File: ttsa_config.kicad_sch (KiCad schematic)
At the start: 11 parts, among them J7 Conn_01x02, SW3 B3U-1000P, SW3 SW_DIP_x09

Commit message: Friendlier sort of scan drive bits, and more doc
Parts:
- R21: now not fitted
- R21: now fitted
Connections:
- net SCS.DRV_{0}: now also R21.1, R21.2; no longer R21.1, R21.2
- net SCS.DRV_{1}: now also R21.1, R21.2; no longer R21.1, R21.2
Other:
- note added: "debounced, 'cause I'm a nice guy"
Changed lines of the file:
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@@
     (effects (font (size 0.8 0.8) (thickness 0.16) bold) (justify left bottom))
+  )
+  (text "debounced, 'cause\nI'm a nice guy" (at 250.19 77.47 90)
+    (effects (font (size 0.8 0.8)) (justify left bottom))
   )
   (text "Latch slow clock\ndivider.  When this is \npulsed, the value present\non in* pins is used to\nconfigure the slow clock\ndivider--neat."
@@
     (effects (font (size 2 2)) (justify left bottom))
   )
-  (label "SCS.setdiv" (at 231.14 76.2 90)
-    (effects (font (size 1.27 1.27)) (justify left bottom))
-  )
-  (label "SCS.DRV_{1}" (at 203.2 76.2 90) (fields_autoplaced)
+  (label "SCS.setdiv" (at 231.14 76.2 90) (fields_autoplaced)
+    (effects (font (size 1.27 1.27)) (justify left bottom))
+  )
+  (label "SCS.DRV_{1}" (at 200.66 76.2 90) (fields_autoplaced)
     (effects (font (size 1.27 1.27)) (justify left bottom))
   )
@@
     (effects (font (size 1.27 1.27)) (justify left bottom))
   )
-  (label "SCS.slowclk" (at 215.9 76.2 90)
+  (label "SCS.slowclk" (at 215.9 76.2 90) (fields_autoplaced)
     (effects (font (size 1.27 1.27)) (justify left bottom))
   )
@@
     (effects (font (size 1.27 1.27)) (justify left bottom))
   )
-  (label "SCS.DRV_{0}" (at 200.66 76.2 90) (fields_autoplaced)
+  (label "SCS.DRV_{0}" (at 203.2 76.2 90) (fields_autoplaced)
     (effects (font (size 1.27 1.27)) (justify left bottom))
   )
@@
   )
   (symbol (lib_id "Device:R_Small") (at 195.58 88.9 180) (unit 1)
-    (in_bom yes) (on_board yes) (dnp no) (fields_autoplaced)
+    (in_bom yes) (on_board yes) (dnp yes) (fields_autoplaced)
     (property "Reference" "R21" (at 194.0814 87.6879 0)
       (effects (font (size 1.27 1.27)) (justify left))
@@
   )
   (symbol (lib_id "Device:R_Small") (at 208.28 88.9 180) (unit 1)
-    (in_bom yes) (on_board yes) (dnp yes) (fields_autoplaced)
+    (in_bom yes) (on_board yes) (dnp no) (fields_autoplaced)
     (property "Reference" "R21" (at 209.7786 87.6879 0)
       (effects (font (size 1.27 1.27)) (justify right))
@@
   )
   (symbol (lib_id "Device:R_Small") (at 195.58 81.28 180) (unit 1)
-    (in_bom yes) (on_board yes) (dnp yes) (fields_autoplaced)
+    (in_bom yes) (on_board yes) (dnp no) (fields_autoplaced)
     (property "Reference" "R21" (at 194.0814 80.0679 0)
       (effects (font (size 1.27 1.27)) (justify left))
@@
   )
   (symbol (lib_id "Device:R_Small") (at 208.28 81.28 180) (unit 1)
-    (in_bom yes) (on_board yes) (dnp no) (fields_autoplaced)
+    (in_bom yes) (on_board yes) (dnp yes) (fields_autoplaced)
     (property "Reference" "R21" (at 209.7786 80.0679 0)
       (effects (font (size 1.27 1.27)) (justify right))

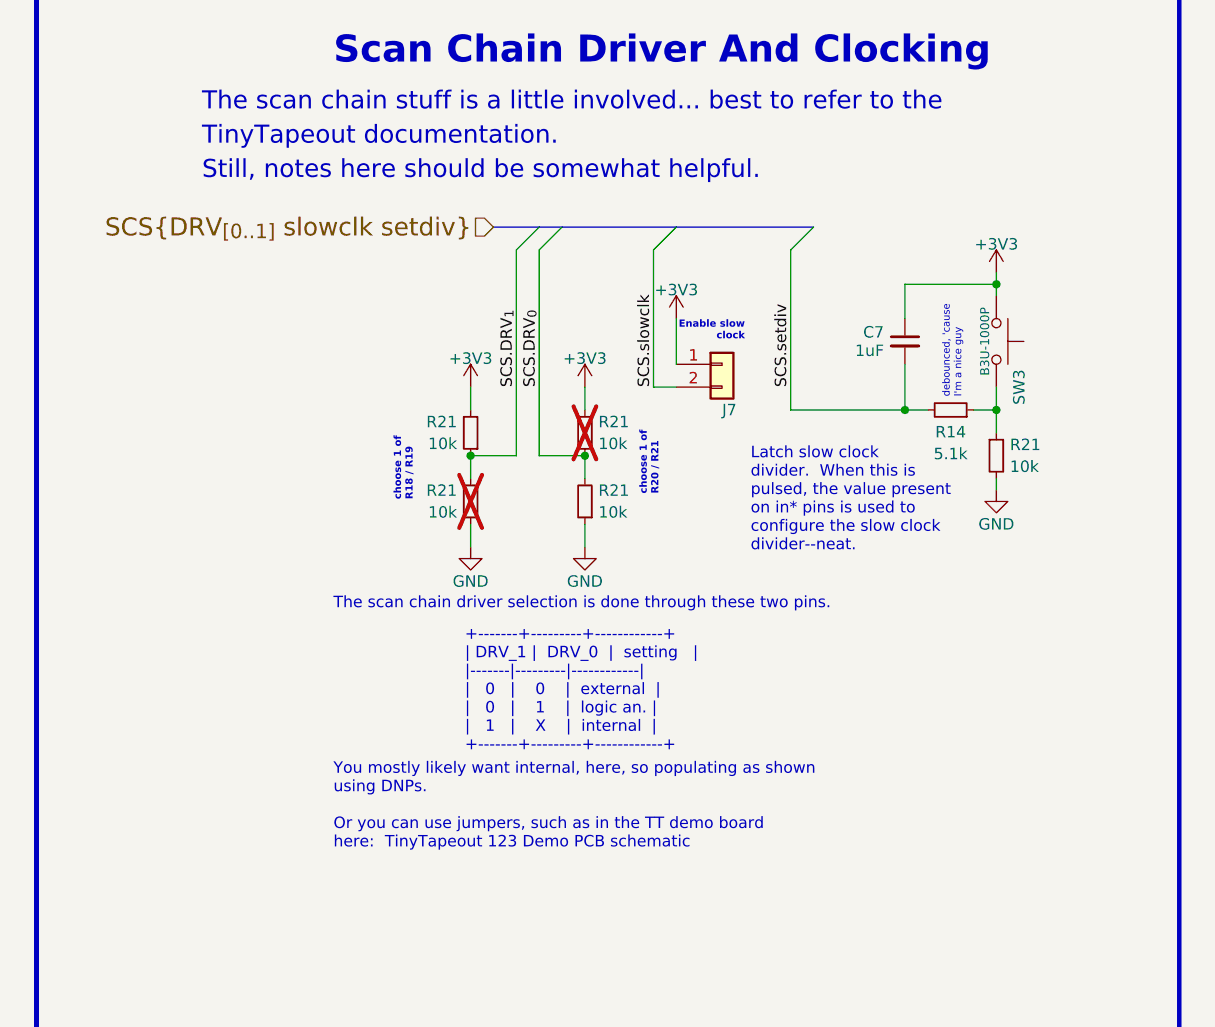
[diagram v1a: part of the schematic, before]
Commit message: Reset rise and slow clock config fixes
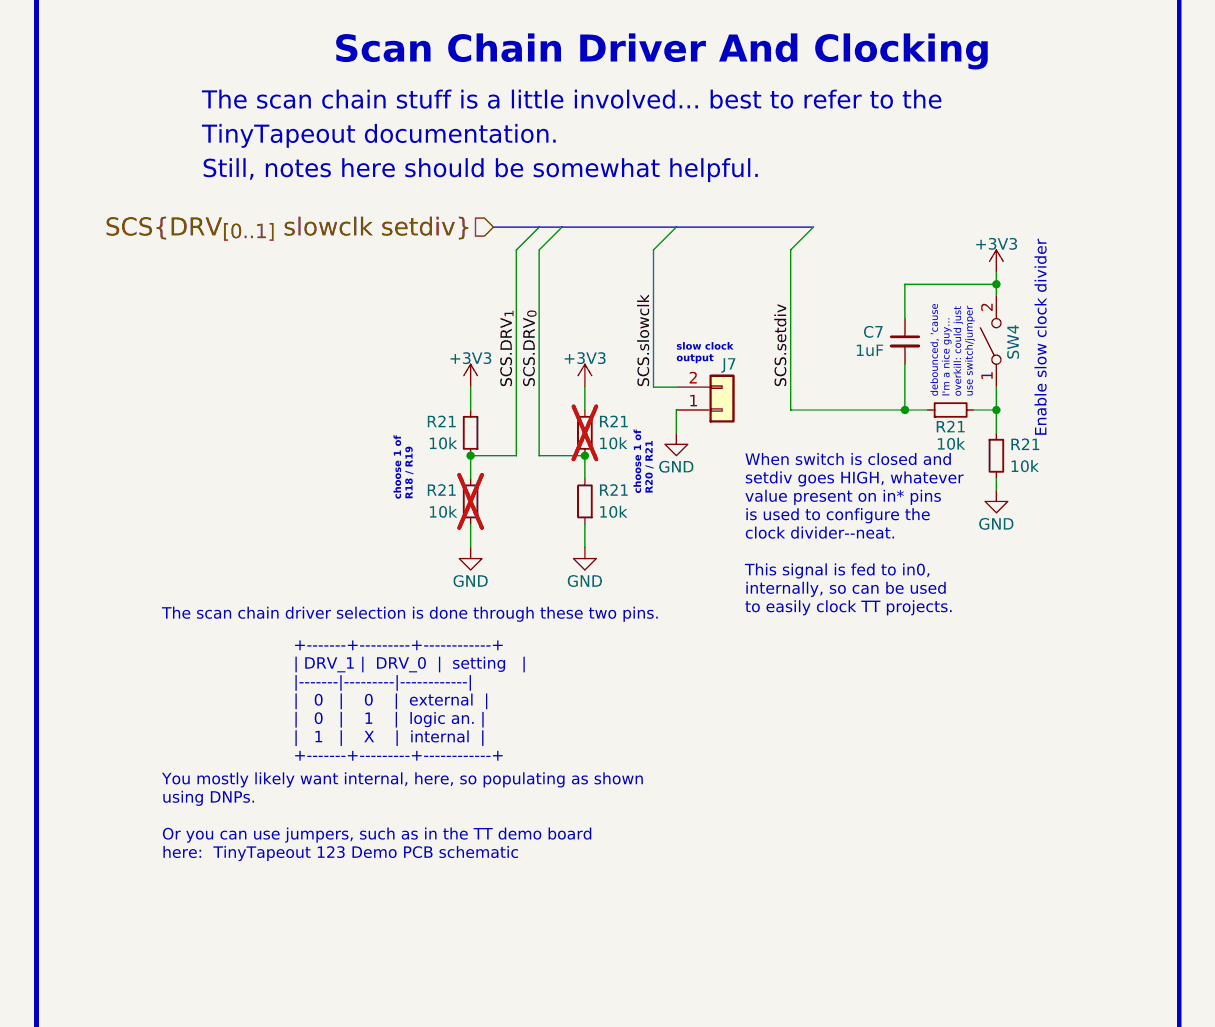
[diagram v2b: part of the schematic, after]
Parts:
- removed R14: 5.1k, Resistor_SMD:R_0603_1608Metric, symbol Device:R_Small
- removed SW3: B3U-1000P, Button_Switch_SMD:SW_SPST_B3U-1000P, symbol Switch:SW_Push
- added R21: 10k, Resistor_SMD:R_0603_1608Metric, symbol Device:R_Small
- added SW4: SPST, symbol Switch:SW_SPST
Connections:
- net +3V3: now also SW4.2 (B); no longer J7.1 (Pin_1)
- net GND: now also J7.1 (Pin_1)
- net SCS.setdiv: now also R21.1
- net at R21.1: now also R21.2, SW4.1 (A)
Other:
- note added: "Enable slow clock divider"
- note added: "When switch is closed and setdiv goes HIGH, whatever value present on in* pins is used to configure the clock divider--neat. This signal is fed to in0, internally, so can be used to easily clock TT projects."
- note added: "debounced, 'cause I'm a nice guy... overkill: could just use switch/jumper"
- note added: "slow clock output"
- note removed: "Enable slow clock"
- note removed: "Latch slow clock divider. When this is pulsed, the value present on in* pins is used to configure the slow clock divider--neat."
- note removed: "debounced, 'cause I'm a nice guy"
- moved on the sheet: J7

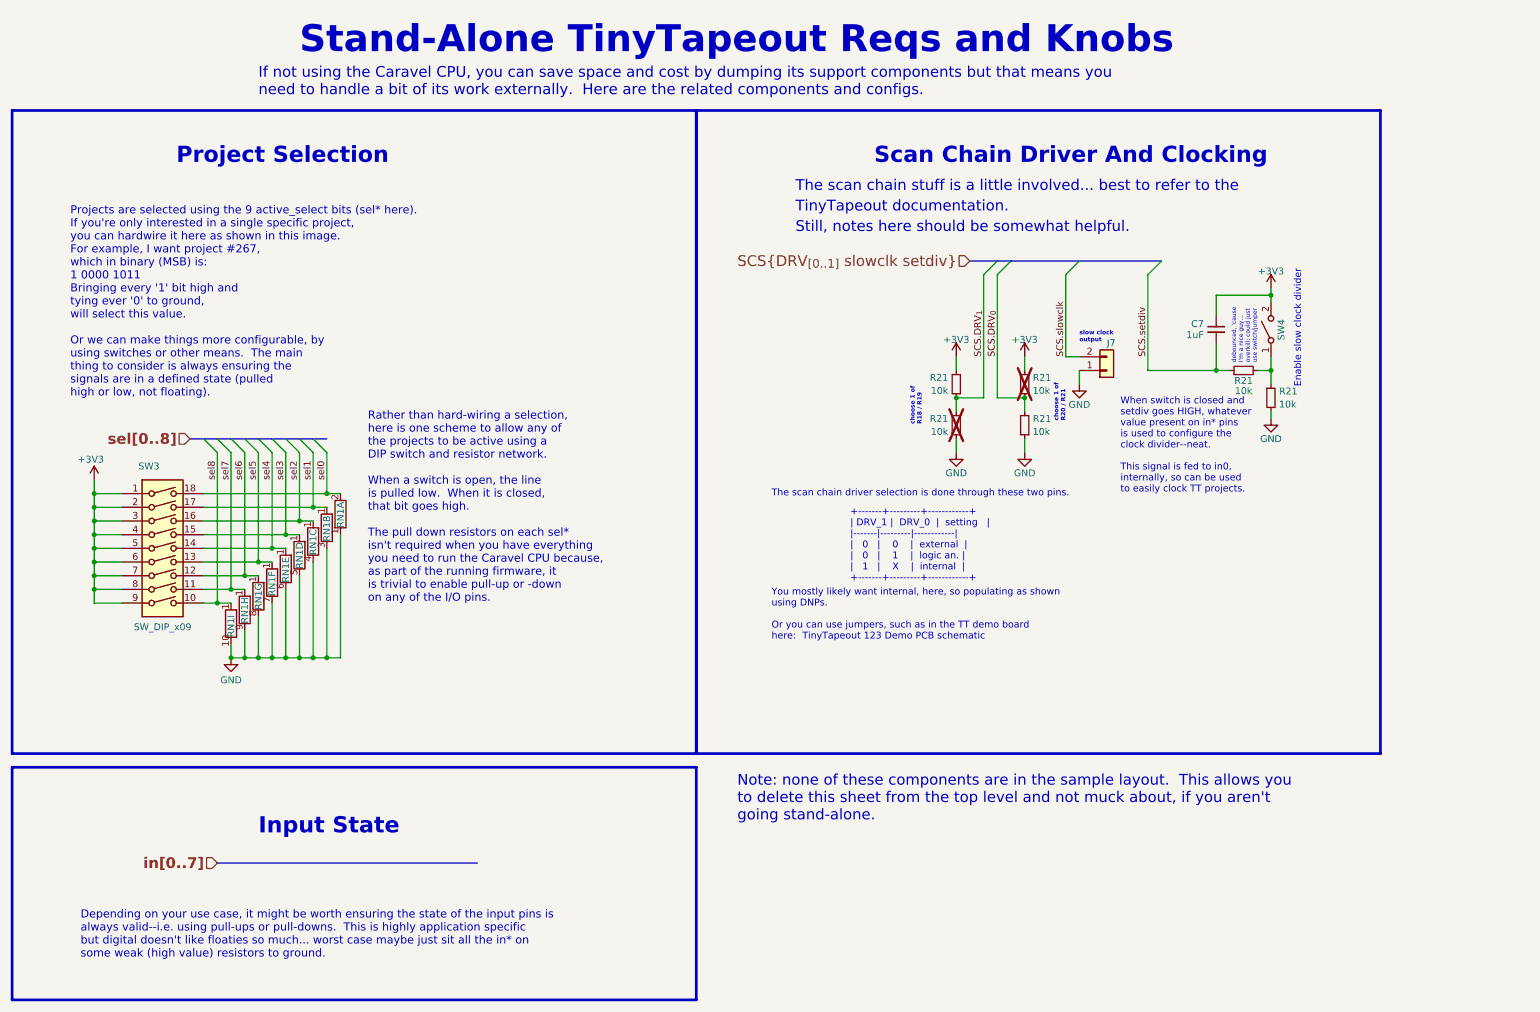
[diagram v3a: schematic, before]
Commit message: minor cleanups and clarifications
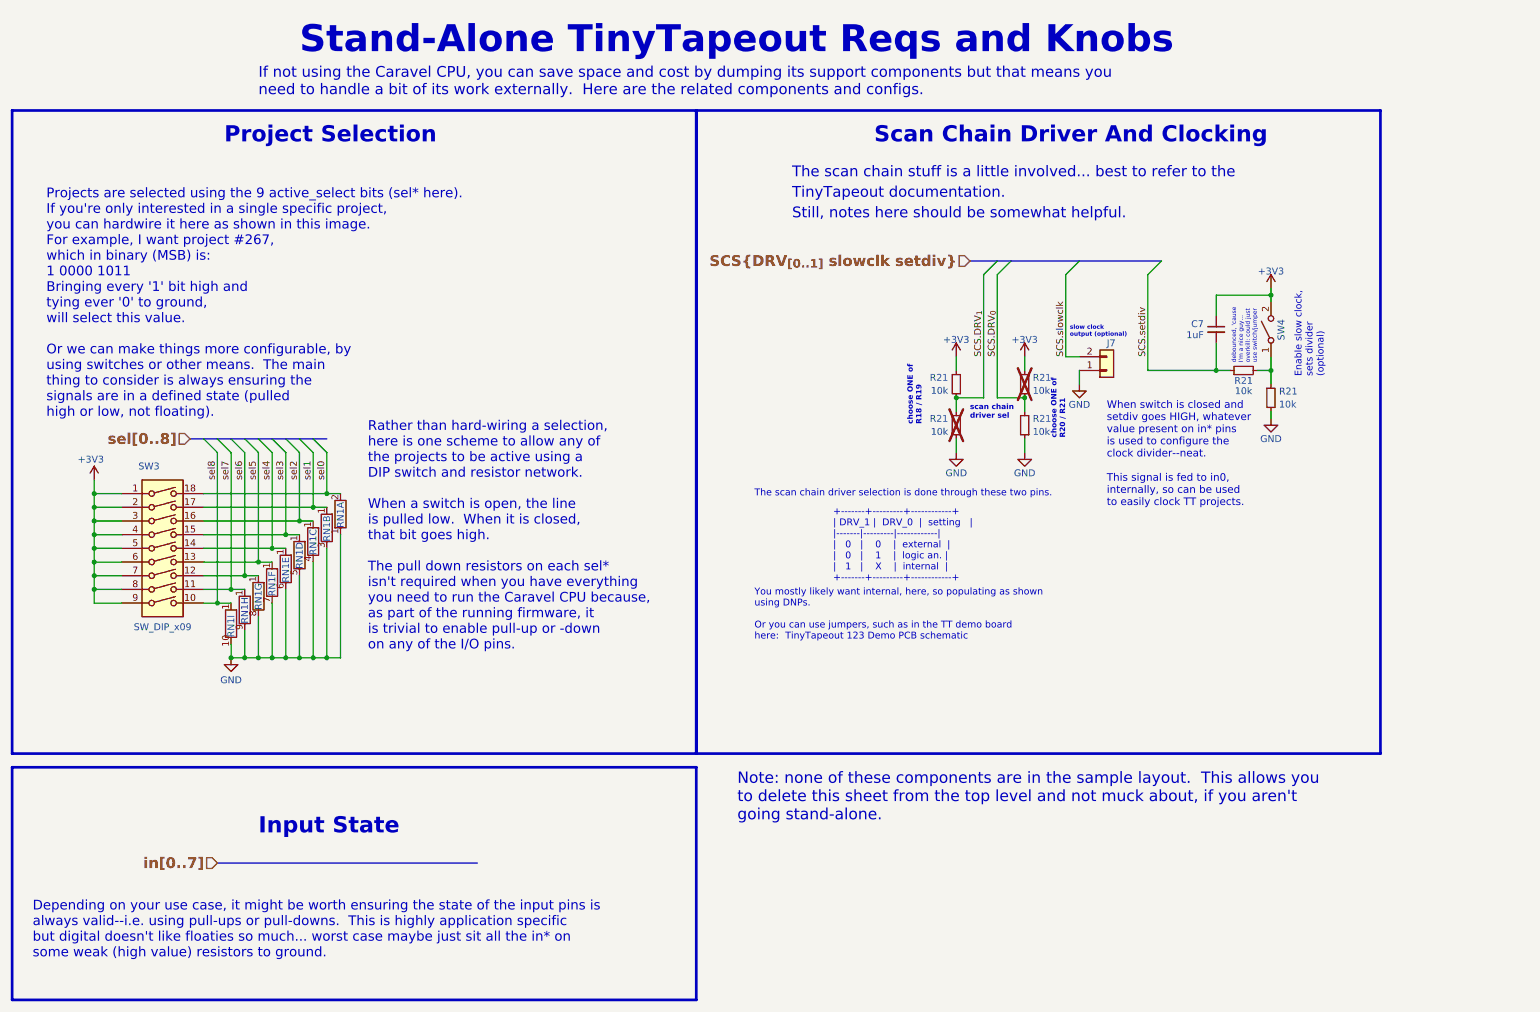
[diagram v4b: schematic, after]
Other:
- note added: "Enable slow clock, sets divider (optional)"
- note added: "choose ONE of R18 / R19"
- note added: "choose ONE of R20 / R21"
- note added: "scan chain driver sel"
- note added: "slow clock output (optional)"
- note removed: "Enable slow clock divider"
- note removed: "choose 1 of R18 / R19"
- note removed: "choose 1 of R20 / R21"
- note removed: "slow clock output"
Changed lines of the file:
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@@
     )
   )
-  (text "choose 1 of\nR20 / R21" (at 215.9 88.265 90)
-    (effects (font (size 0.8 0.8) (thickness 0.16) bold) (justify left bottom))
+  (text "choose ONE of\nR20 / R21" (at 215.9 91.44 90)
+    (effects (font (size 1 1) (thickness 0.16) bold) (justify left bottom))
   )
-  (text "TinyTapeout 123 Demo PCB schematic" (at 167.005 128.905 0)
+  (text "TinyTapeout 123 Demo PCB schematic" (at 163.83 128.905 0)
     (effects (font (size 1.27 1.27)) (justify left bottom) (href "https://github.com/TinyTapeout/tt123-demo-pcb/blob/main/doc/mpw-mb1-v2-2-2.pdf"))
+  )
+  (text "scan chain\ndriver sel" (at 198.12 87.884 0)
+    (effects (font (size 1 1) (thickness 0.16) bold) (justify left bottom))
   )
   (text "Input State" (at 66.04 165.1 0)
@@
   )
   (text "Rather than hard-wiring a selection, \nhere is one scheme to allow any of \nthe projects to be active using a \nDIP switch and resistor network.\n\nWhen a switch is open, the line \nis pulled low.  When it is closed, \nthat bit goes high.  \n\nThe pull down resistors on each sel*\nisn't required when you have everything\nyou need to run the Caravel CPU because,\nas part of the running firmware, it \nis trivial to enable pull-up or -down \non any of the I/O pins."
-    (at 86.36 121.92 0)
-    (effects (font (size 1.5 1.5)) (justify left bottom))
+    (at 86.36 130.81 0)
+    (effects (font (size 1.8 1.8)) (justify left bottom))
   )
   (text "Projects are selected using the 9 active_select bits (sel* here).  \nIf you're only interested in a single specific project, \nyou can hardwire it here as shown in this image.\nFor example, I want project #267,\nwhich in binary (MSB) is: \n1 0000 1011 \nBringing every '1' bit high and \ntying ever '0' to ground, \nwill select this value.\n\nOr we can make things more configurable, by \nusing switches or other means.  The main\nthing to consider is always ensuring the \nsignals are in a defined state (pulled \nhigh or low, not floating)."
-    (at 31.115 83.82 0)
-    (effects (font (size 1.5 1.5)) (justify left bottom))
+    (at 26.67 87.63 0)
+    (effects (font (size 1.8 1.8)) (justify left bottom))
   )
-  (text "slow clock\noutput" (at 218.44 73.66 0)
+  (text "slow clock\noutput (optional)" (at 216.662 72.644 0)
     (effects (font (size 0.8 0.8) (thickness 0.16) bold) (justify left bottom))
   )
   (text "The scan chain driver selection is done through these two pins.\n\n\n\n\n\n\n\n\nYou mostly likely want internal, here, so populating as shown \nusing DNPs.\n\nOr you can use jumpers, such as in the TT demo board \nhere:"
-    (at 161.29 128.905 0)
+    (at 158.115 128.905 0)
     (effects (font (size 1.27 1.27)) (justify left bottom))
   )
-  (text "Enable slow clock divider" (at 259.715 81.915 90)
+  (text "Enable slow clock,\nsets divider \n(optional)" (at 263.906 80.01 90)
     (effects (font (size 1.27 1.27)) (justify left bottom))
   )
@@
     (effects (font (size 5 5) (thickness 0.6) bold) (justify left bottom))
   )
-  (text "Project Selection" (at 50.8 40.64 0)
+  (text "Project Selection" (at 59.69 36.83 0)
     (effects (font (size 3 3) (thickness 0.6) bold) (justify left bottom))
   )
   (text "The scan chain stuff is a little involved... best to refer to the \n"
-    (at 165.735 45.72 0)
+    (at 165.1 43.18 0)
     (effects (font (size 2 2)) (justify left bottom))
   )
-  (text "Scan Chain Driver And Clocking" (at 180.34 40.64 0)
+  (text "Scan Chain Driver And Clocking" (at 180.34 36.83 0)
     (effects (font (size 3 3) (thickness 0.6) bold) (justify left bottom))
   )
-  (text "Still, notes here should be somewhat helpful." (at 165.735 53.34 0)
+  (text "Still, notes here should be somewhat helpful." (at 165.1 50.8 0)
     (effects (font (size 2 2)) (justify left bottom))
   )
   (text "+-------+---------+------------+\n| DRV_1 |  DRV_0  |  setting   |\n|-------|---------|------------|\n|   0   |    0    |  external  |\n|   0   |    1    |  logic an. |\n|   1   |    X    |  internal  |\n+-------+---------+------------+"
-    (at 175.895 118.11 0)
+    (at 172.72 118.11 0)
     (effects (font (face "Bitstream Vera Sans Mono") (size 1.27 1.27)) (justify left bottom))
   )
@@
   )
   (text "Depending on your use case, it might be worth ensuring the state of the input pins is \nalways valid--i.e. using pull-ups or pull-downs.  This is highly application specific \nbut digital doesn't like floaties so much... worst case maybe just sit all the in* on \nsome weak (high value) resistors to ground."
-    (at 33.02 187.96 0)
-    (effects (font (size 1.5 1.5)) (justify left bottom))
+    (at 24.13 187.96 0)
+    (effects (font (size 1.8 1.8)) (justify left bottom))
   )
-  (text "TinyTapeout documentation." (at 165.735 49.53 0)
+  (text "TinyTapeout documentation." (at 165.1 46.99 0)
     (effects (font (size 2 2)) (justify left bottom) (href "https://github.com/tinytapeout/tinytapeout-mpw7/blob/mpw7/INFO.md"))
   )
-  (text "choose 1 of\nR18 / R19" (at 189.23 88.9 90)
-    (effects (font (size 0.8 0.8) (thickness 0.16) bold) (justify left bottom))
+  (text "choose ONE of\nR18 / R19" (at 189.23 88.9 90)
+    (effects (font (size 1 1) (thickness 0.16) bold) (justify left bottom))
   )
   (text "debounced, 'cause\nI'm a nice guy...\noverkill: could just\nuse switch/jumper"
@@
   )
   (text "When switch is closed and \nsetdiv goes HIGH, whatever \nvalue present on in* pins\nis used to configure the \nclock divider--neat.\n\nThis signal is fed to in0,\ninternally, so can be used\nto easily clock TT projects."
-    (at 226.06 101.6 0)
-    (effects (font (size 1.27 1.27)) (justify left bottom))
+    (at 223.52 104.14 0)
+    (effects (font (size 1.4 1.4)) (justify left bottom))
   )
   (text "Note: none of these components are in the sample layout.  This allows you\nto delete this sheet from the top level and not muck about, if you aren't \ngoing stand-alone."
     (at 154.94 162.56 0)
-    (effects (font (size 2 2)) (justify left bottom))
+    (effects (font (size 2.1 2.1)) (justify left bottom))
   )
   (label "SCS.setdiv" (at 231.14 76.2 90) (fields_autoplaced)
@@
   )
   (hierarchical_label "SCS{DRV_{[0..1]} slowclk setdiv}" (shape input) (at 198.12 58.42 180) (fields_autoplaced)
-    (effects (font (size 2 2) (color 194 0 194 1)) (justify right))
+    (effects (font (size 2 2) (thickness 0.4) bold (color 194 0 194 1)) (justify right))
   )
   (symbol (lib_id "Connector_Generic:Conn_01x02") (at 223.52 78.74 0) (mirror x) (unit 1)
